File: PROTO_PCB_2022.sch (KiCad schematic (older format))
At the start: 22 parts

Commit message: Minor changes
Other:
- note added: "To Do:\n1. Add Mini ATtiny85 board\n2. Add Oxygen Sensor\n4. ECU has to kill electronics too (check and implement this)\n5. Brakelight Enable - not from a button, but from the reed switch (consider an alternative method) - Sarah to find a reed switch\n\n(NEW) 6. Add an extra connection terminal for the 12V battery in case"
- note removed: "Starter Motor Enable 12V should come \nfrom small battery (to power coil) - Talisha to ask Luke"
- note removed: "To Do:\n1. Add 5V step down chip\n2. Oxygen Sensor\n3. Check that the current of MOSFET is enough for horn and brake lights (get datasheet for horn and brake lights)\n4. ECU has to kill electronics too (check and implement this)\n5. Brakelight Enable - not from a button, but from the reed switch (consider an alternative method) - Sarah to find a reed switch"
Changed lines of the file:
@@
 Connection ~ 2700 8000
 Text Notes 5800 1150 0    50   ~ 0
-To Do:\n1. Add 5V step down chip\n2. Oxygen Sensor\n3. Check that the current of MOSFET is enough for horn and brake lights (get datasheet for horn and brake lights)\n4. ECU has to kill electronics too (check and implement this)\n5. Brakelight Enable - not from a button, but from the reed switch (consider an alternative method) - Sarah to find a reed switch
+To Do:\n1. Add Mini ATtiny85 board\n2. Add Oxygen Sensor\n4. ECU has to kill electronics too (check and implement this)\n5. Brakelight Enable - not from a button, but from the reed switch (consider an alternative method) - Sarah to find a reed switch\n\n(NEW) 6. Add an extra connection terminal for the 12V battery in case
 $Comp
 L Switch:SW_Push SW?
@@
 	0    -1   -1   0
 $EndComp
-Text Notes 7400 6200 0    50   ~ 0
+Text Notes 6250 5950 0    50   ~ 0
 SHOULD WE SEPARATE SIGNAL_12V FROM POWER_12V?
-Text Notes 7400 6050 0    50   ~ 0
-Starter Motor Enable 12V should come \nfrom small battery (to power coil) - Talisha to ask Luke
-$Comp
-L power:GND #PWR?
+$Comp
+L power:GND #PWR?

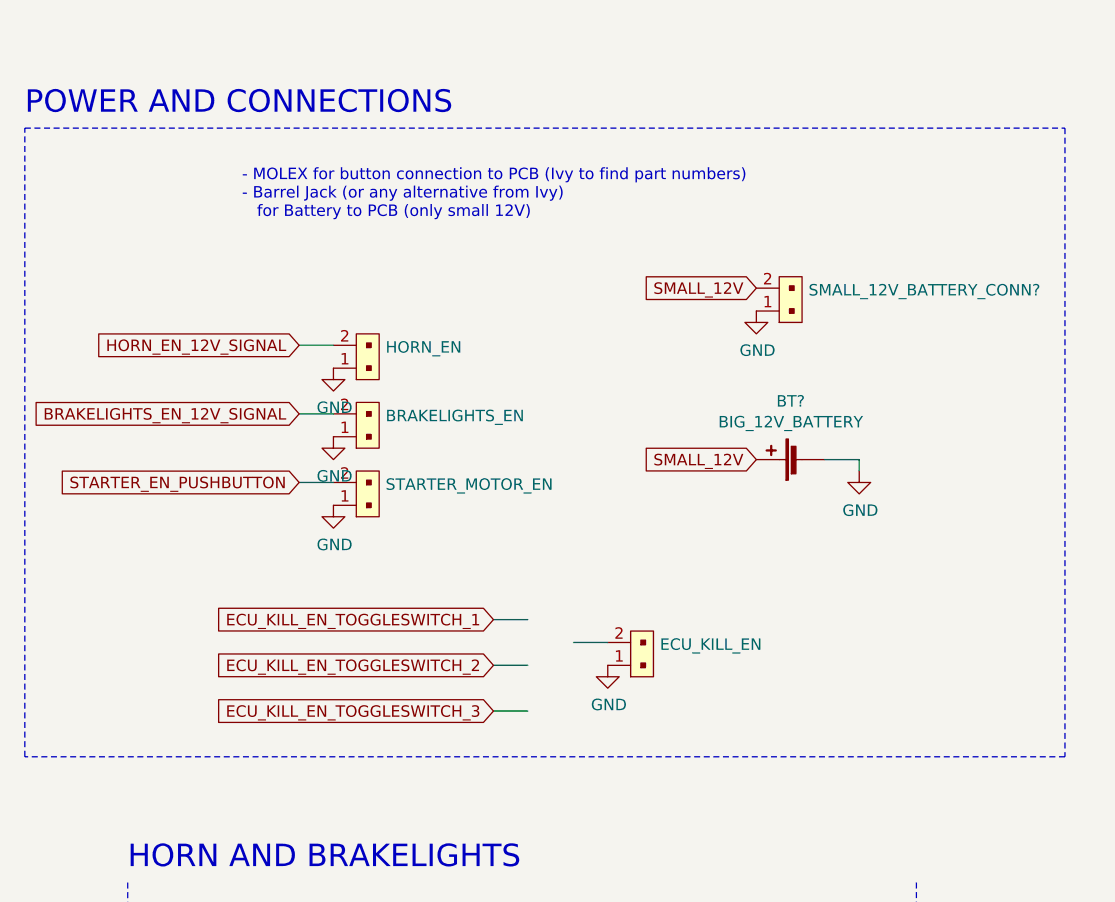
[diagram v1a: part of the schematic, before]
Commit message: Added ECU molex
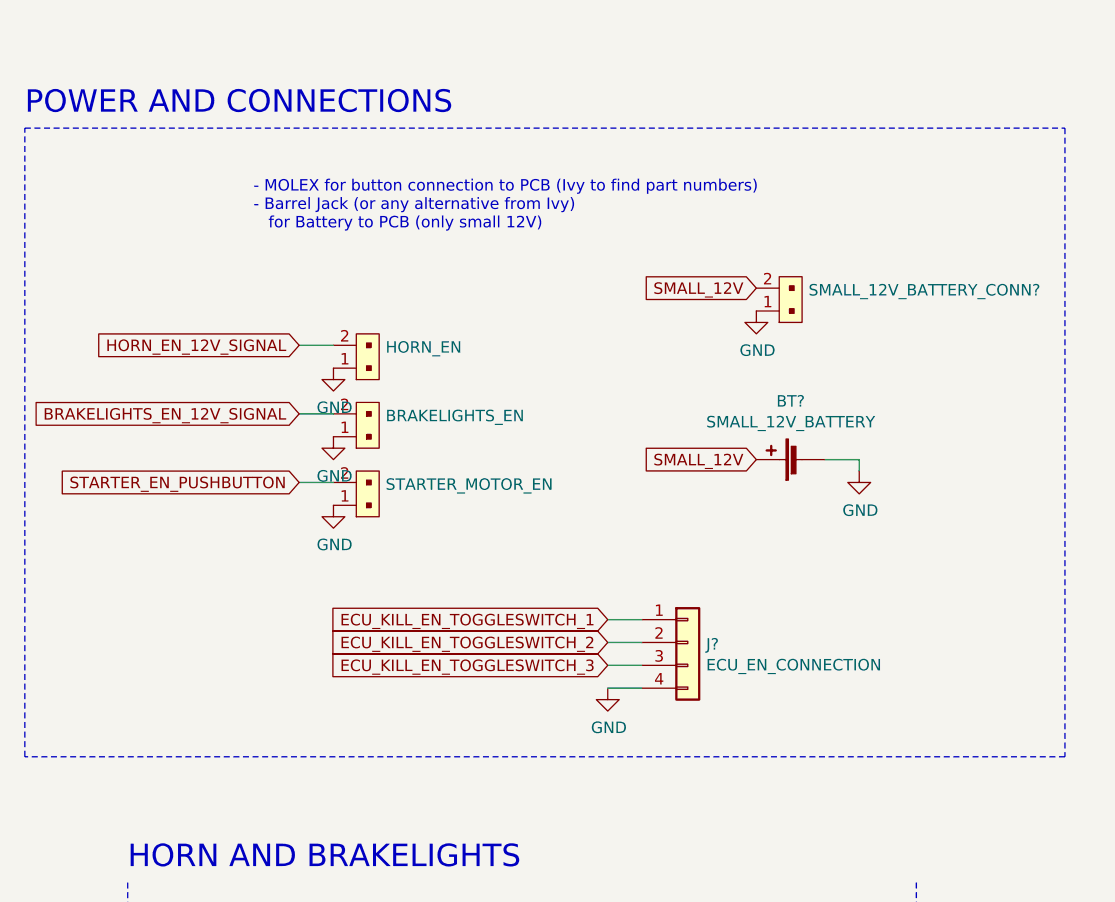
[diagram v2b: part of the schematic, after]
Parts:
- removed ECU_KILL_EN: Conn_?, symbol PROTO_PCB_2022-rescue:B2B-PH-K-S_LF__SN_-dk_Rectangular-Connectors-Headers-Male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
- added J?: ECU_EN_CONNECTION, Connector_Molex:Molex_CLIK-Mate_505405-0470_1x04-1MP_P1.50mm_Vertical, symbol Connector_Generic:Conn_01x04
- BT?: value BIG_12V_BATTERY -> SMALL_12V_BATTERY
- HORN_EN: footprint (none) -> Connector_Molex:Molex_CLIK-Mate_502443-0270_1x02-1MP_P2.00mm_Vertical; DigiKeyPN (none) -> WM10606CT-ND; MPN (none) -> 5033950410
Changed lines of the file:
@@
 STARTER_EN_PUSHBUTTON
-$Comp
-L PROTO_PCB_2022-rescue:B2B-PH-K-S_LF__SN_-dk_Rectangular-Connectors-Headers-Male-Pins-Proto-PCB's-combined-rescue-Proto-PCB's-combined-rescue ECU_KILL_EN
-U 1 1 618FB70C
-P 3450 3450
-F 0 "ECU_KILL_EN" V 3541 3322 50  0000 R CNN
-F 1 "Conn_?" V 3450 3322 50  0001 R CNN
-F 2 "" H 3650 3650 60  0001 L CNN
-F 3 "" H 3650 3750 60  0001 L CNN
-F 4 "" H 3650 3850 60  0001 L CNN "DigiKeyPN"
-F 5 "" H 3650 3950 60  0001 L CNN "MPN"
-	1    3450 3450
-	0    -1   -1   0
-$EndComp
 $Comp
 L Device:R R2
@@
 F 0 "HORN_EN" V 2341 2022 50  0000 R CNN
 F 1 "Conn_?" V 2250 2022 50  0001 R CNN
-F 2 "" H 2450 2350 60  0001 L CNN
-F 3 "" H 2450 2450 60  0001 L CNN
-F 4 "" H 2450 2550 60  0001 L CNN "DigiKeyPN"
-F 5 "" H 2450 2650 60  0001 L CNN "MPN"
+F 2 "Connector_Molex:Molex_CLIK-Mate_502443-0270_1x02-1MP_P2.00mm_Vertical" H 2450 2350 60  0001 L CNN
+F 3 "http://www.literature.molex.com/SQLImages/kelmscott/Molex/PDF_Images/987650-3302.PDF" H 2450 2450 60  0001 L CNN
+F 4 "WM10606CT-ND" H 2450 2550 60  0001 L CNN "DigiKeyPN"
+F 5 "5033950410" H 2450 2650 60  0001 L CNN "MPN"
 	1    2250 2150
 	0    -1   -1   0
@@
 L power:GND #PWR?
 U 1 1 61EE9E38
-P 3350 3450
-F 0 "#PWR?" H 3350 3200 50  0001 C CNN
-F 1 "GND" H 3355 3277 50  0000 C CNN
-F 2 "" H 3350 3450 50  0001 C CNN
-F 3 "" H 3350 3450 50  0001 C CNN
-	1    3350 3450
+P 3350 3550
+F 0 "#PWR?" H 3350 3300 50  0001 C CNN
+F 1 "GND" H 3355 3377 50  0000 C CNN
+F 2 "" H 3350 3550 50  0001 C CNN
+F 3 "" H 3350 3550 50  0001 C CNN
+	1    3350 3550
 	1    0    0    -1
 $EndComp
@@
 HORN_EN_12V_SIGNAL
 Wire Wire Line
-	3200 3350 3350 3350
+	3350 3550 3500 3550
 Wire Wire Line
 	2000 2050 2150 2050
@@
 Wire Wire Line
 	7750 4300 7750 4250
-Text Notes 1750 1500 0    50   ~ 0
+Text Notes 1800 1550 0    50   ~ 0
 - MOLEX for button connection to PCB (Ivy to find part numbers)\n- Barrel Jack (or any alternative from Ivy) \n   for Battery to PCB (only small 12V)
 $Comp
@@
 Text GLabel 4000 1800 0    50   Input ~ 0
 SMALL_12V
+$Comp
+L power:GND #PWR?
+U 1 1 61EE2CFA
+P 4450 2600
+F 0 "#PWR?" H 4450 2350 50  0001 C CNN
+F 1 "GND" H 4455 2427 50  0000 C CNN
+F 2 "" H 4450 2600 50  0001 C CNN
+F 3 "" H 4450 2600 50  0001 C CNN
+	1    4450 2600
+	1    0    0    -1
+$EndComp
+Wire Wire Line
+	4450 2550 4450 2600
+Wire Wire Line
+	4300 2550 4450 2550
+$Comp
+L Device:Battery_Cell BT?
+U 1 1 61EB6EF2
+P 4200 2550
+F 0 "BT?" V 4455 2600 50  0000 C CNN
+F 1 "SMALL_12V_BATTERY" V 4364 2600 50  0000 C CNN
+F 2 "" V 4200 2610 50  0001 C CNN
+F 3 "~" V 4200 2610 50  0001 C CNN
+	1    4200 2550
+	0    -1   -1   0
+$EndComp
+Text GLabel 4000 2550 0    50   Input ~ 0
+SMALL_12V
+Wire Wire Line
+	7100 2600 7250 2600
+Wire Wire Line
+	7100 2400 7250 2400
+Wire Wire Line
+	7250 2400 7250 2600
+Connection ~ 7250 2600
+Wire Wire Line
+	7250 2600 7600 2600
+Wire Wire Line
+	7100 2800 7250 2800
+Wire Wire Line
+	7250 2800 7250 2600
+Text GLabel 3350 3350 0    50   Input ~ 0
+ECU_KILL_EN_TOGGLESWITCH_2
+Text GLabel 3350 3450 0    50   Input ~ 0
+ECU_KILL_EN_TOGGLESWITCH_3
+Text GLabel 3350 3250 0    50   Input ~ 0
+ECU_KILL_EN_TOGGLESWITCH_1
+Wire Wire Line
+	3350 3250 3500 3250
+Wire Wire Line
+	3350 3350 3500 3350
+Wire Wire Line
+	3350 3450 3500 3450
+$Comp
+L Switch:SW_Push SW?
+U 1 1 61F362BE
+P 9400 3000
+F 0 "SW?" H 9400 3285 50  0000 C CNN
+F 1 "ECU_KILL_TOGGLESWITCH_2" H 9400 3194 50  0000 C CNN
+F 2 "" H 9400 3200 50  0001 C CNN
+F 3 "~" H 9400 3200 50  0001 C CNN
+	1    9400 3000
+	1    0    0    -1
+$EndComp
+Text GLabel 9200 3000 0    50   Input ~ 0
+SMALL_12V
+Text GLabel 9600 3000 2    50   Input ~ 0
+ECU_KILL_EN_TOGGLESWITCH_2
+$Comp
+L Switch:SW_Push SW?
+U 1 1 61F3728F
+P 9400 3400
+F 0 "SW?" H 9400 3685 50  0000 C CNN
+F 1 "ECU_KILL_TOGGLESWITCH_3" H 9400 3594 50  0000 C CNN
+F 2 "" H 9400 3600 50  0001 C CNN
+F 3 "~" H 9400 3600 50  0001 C CNN
+	1    9400 3400
+	1    0    0    -1
+$EndComp
+Text GLabel 9200 3400 0    50   Input ~ 0
+SMALL_12V
+Text GLabel 9600 3400 2    50   Input ~ 0
+ECU_KILL_EN_TOGGLESWITCH_3
+Wire Notes Line
+	5750 1750 11000 1750
+Wire Notes Line
+	11000 1750 11000 6300
+Wire Notes Line
+	11000 6300 5750 6300
+Wire Notes Line
+	5750 6300 5750 1750
+Wire Notes Line
+	800  1100 5350 1100
+Wire Notes Line
+	5350 1100 5350 3850
+Wire Notes Line
+	5350 3850 800  3850
+Wire Notes Line
+	800  3850 800  1100
+Text Notes 5750 1700 0    98   ~ 0
+STARTER AND ECU\n
+Text Notes 800  1050 0    98   ~ 0
+POWER AND CONNECTIONS\n
 $Comp
 L PROTO_PCB_2022-rescue:B2B-PH-K-S_LF__SN_-dk_Rectangular-Connectors-Headers-Male-Pins-Proto-PCB's-combined-rescue-Proto-PCB's-combined-rescue SMALL_12V_BATTERY_CONN?
@@
 $EndComp
 $Comp
-L power:GND #PWR?
-U 1 1 61EE2CFA
-P 4450 2600
-F 0 "#PWR?" H 4450 2350 50  0001 C CNN
-F 1 "GND" H 4455 2427 50  0000 C CNN
-F 2 "" H 4450 2600 50  0001 C CNN
-F 3 "" H 4450 2600 50  0001 C CNN
-	1    4450 2600
-	1    0    0    -1
-$EndComp
-Wire Wire Line
-	4450 2550 4450 2600
-Wire Wire Line
-	4300 2550 4450 2550
-$Comp
-L Device:Battery_Cell BT?
-U 1 1 61EB6EF2
-P 4200 2550
-F 0 "BT?" V 4455 2600 50  0000 C CNN
-F 1 "BIG_12V_BATTERY" V 4364 2600 50  0000 C CNN
-F 2 "" V 4200 2610 50  0001 C CNN
-F 3 "~" V 4200 2610 50  0001 C CNN
-	1    4200 2550
-	0    -1   -1   0
-$EndComp
-Text GLabel 4000 2550 0    50   Input ~ 0
-SMALL_12V
-Wire Wire Line
-	7100 2600 7250 2600
-Wire Wire Line
-	7100 2400 7250 2400
-Wire Wire Line
-	7250 2400 7250 2600
-Connection ~ 7250 2600
-Wire Wire Line
-	7250 2600 7600 2600
-Wire Wire Line
-	7100 2800 7250 2800
-Wire Wire Line
-	7250 2800 7250 2600
-Text GLabel 2850 3450 0    50   Input ~ 0
-ECU_KILL_EN_TOGGLESWITCH_2
-Text GLabel 2850 3650 0    50   Input ~ 0
-ECU_KILL_EN_TOGGLESWITCH_3
-Text GLabel 2850 3250 0    50   Input ~ 0
-ECU_KILL_EN_TOGGLESWITCH_1
-Wire Wire Line
-	2850 3250 3000 3250
-Wire Wire Line
-	2850 3450 3000 3450
-Wire Wire Line
-	2850 3650 3000 3650
-$Comp
-L Switch:SW_Push SW?
-U 1 1 61F362BE
-P 9400 3000
-F 0 "SW?" H 9400 3285 50  0000 C CNN
-F 1 "ECU_KILL_TOGGLESWITCH_2" H 9400 3194 50  0000 C CNN
-F 2 "" H 9400 3200 50  0001 C CNN
-F 3 "~" H 9400 3200 50  0001 C CNN
-	1    9400 3000
-	1    0    0    -1
-$EndComp
-Text GLabel 9200 3000 0    50   Input ~ 0
-SMALL_12V
-Text GLabel 9600 3000 2    50   Input ~ 0
-ECU_KILL_EN_TOGGLESWITCH_2
-$Comp
-L Switch:SW_Push SW?
-U 1 1 61F3728F
-P 9400 3400
-F 0 "SW?" H 9400 3685 50  0000 C CNN
-F 1 "ECU_KILL_TOGGLESWITCH_3" H 9400 3594 50  0000 C CNN
-F 2 "" H 9400 3600 50  0001 C CNN
-F 3 "~" H 9400 3600 50  0001 C CNN
-	1    9400 3400
-	1    0    0    -1
-$EndComp
-Text GLabel 9200 3400 0    50   Input ~ 0
-SMALL_12V
-Text GLabel 9600 3400 2    50   Input ~ 0
-ECU_KILL_EN_TOGGLESWITCH_3
-Wire Notes Line
-	5750 1750 11000 1750
-Wire Notes Line
-	11000 1750 11000 6300
-Wire Notes Line
-	11000 6300 5750 6300
-Wire Notes Line
-	5750 6300 5750 1750
-Wire Notes Line
-	800  1100 5350 1100
-Wire Notes Line
-	5350 1100 5350 3850
-Wire Notes Line
-	5350 3850 800  3850
-Wire Notes Line
-	800  3850 800  1100
-Text Notes 5750 1700 0    98   ~ 0
-STARTER AND ECU\n
-Text Notes 800  1050 0    98   ~ 0
-POWER AND CONNECTIONS\n
+L Connector_Generic:Conn_01x04 J?
+U 1 1 61E4C7B0
+P 3700 3350
+F 0 "J?" H 3780 3342 50  0000 L CNN
+F 1 "ECU_EN_CONNECTION" H 3780 3251 50  0000 L CNN
+F 2 "Connector_Molex:Molex_CLIK-Mate_505405-0470_1x04-1MP_P1.50mm_Vertical" H 3700 3350 50  0001 C CNN
+F 3 "~" H 3700 3350 50  0001 C CNN
+	1    3700 3350
+	1    0    0    -1
+$EndComp
 $EndSCHEMATC

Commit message: Continued development
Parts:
- removed BT?: SMALL_12V_BATTERY, symbol Device:Battery_Cell
- removed R?: HORN, symbol Device:R
- removed R?: BRAKELIGHTS, symbol Device:R
- removed R?: STARTER MOTOR, symbol Device:R
- removed STARTER_FUSE: Fuse_1, Fuse:Fuseholder_Blade_Mini_Keystone_3568, symbol Device:Fuse
- removed SW?: BRAKELIGHTS_BUTTON???, symbol Switch:SW_Push
- removed SW?: HORN_PUSHBUTTON, symbol Switch:SW_Push
- removed SW?: ECU_KILL_TOGGLESWITCH_1, symbol Switch:SW_Push
- removed SW?: STARTERMOTOR_BUTTON, symbol Switch:SW_Push
- removed SW?: ECU_KILL_TOGGLESWITCH_2, symbol Switch:SW_Push
- removed SW?: ECU_KILL_TOGGLESWITCH_3, symbol Switch:SW_Push
- added IVY_UPDATE_EXTRA_POWER: Conn_?, symbol PROTO_PCB_2022-rescue:B2B-PH-K-S_LF__SN_-dk_Rectangular-Connectors-Headers-Male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
- added J?: ECU_EN_CONNECTION, Connector_Molex:Molex_CLIK-Mate_505405-0470_1x04-1MP_P1.50mm_Vertical, symbol Connector_Generic:Conn_01x04
- added U?: ATtiny85-20MU, Package_DFN_QFN:QFN-20-1EP_4x4mm_P0.5mm_EP2.6x2.6mm, symbol MCU_Microchip_ATtiny:ATtiny85-20MU
- gave numbers to parts that had none: 4
- renumbered BRAKELIGHTS_EN to BRAKELIGHTS_EN1, BRAKELIGHTS_MOSFET to BRAKELIGHTS_MOSFET1, HORN_EN to HORN_EN1, HORN_MOSFET to HORN_MOSFET1, STARTER_MOTOR_EN to STARTER_MOTOR_EN1
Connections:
- net GND: now also IVY_UPDATE_EXTRA_POWER.1, J?.4 (Pin_4)
- net SMALL_12V: now also IVY_UPDATE_EXTRA_POWER.2, J?.1 (Pin_1)
- new net: U?.21 (GND), U?.8 (GND)
- new net O2_ANALOG_READING_SIGNAL: J?.2 (Pin_2), U?.12 (PB1)
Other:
- note added: "3 connection-Molex: PWR (12V), GND, SIG(O2)"
- note added: "To Do:\n1. DONE - Add Mini ATtiny85 board\n2. DONE - Add Oxygen Sensor (header)\n6. IVY - Add an extra connection terminal for the 12V battery in case"
- note removed: "To Do:\n1. Add Mini ATtiny85 board\n2. Add Oxygen Sensor\n4. ECU has to kill electronics too (check and implement this)\n5. Brakelight Enable - not from a button, but from the reed switch (consider an alternative method) - Sarah to find a reed switch\n\n(NEW) 6. Add an extra connection terminal for the 12V battery in case"
- moved on the sheet: BRAKELIGHTS_MOSFET1, HORN_MOSFET1, J1, R1, R2, SMALL_12V_BATTERY_CONN1
